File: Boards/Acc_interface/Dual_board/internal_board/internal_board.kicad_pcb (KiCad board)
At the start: 4 copper layers, 85 x 70 mm, 7 parts, among them J2 MM_F_RA_20, J3 MM_F_RA_04, J4 MM_F_RA_14, J5 MM_F_RA_06, J6 MicroFit_RA_10, J7 SS-126-G-2, J8 SS-126-G-2

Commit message: added silkscreen to all acc interface boards
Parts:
- added G***: LOGO, footprints:Olin_O, B.Cu at (134.6, 54.6)
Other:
- board text added: "AIR Control"
- board text added: "Accumulator Interface (Internal) Rev 1 Bryce Mann"
- board text added: "BMS Core"
- board text added: "IMD Latch"
- board text added: "Shutdown"
- board text added: "TSAL"
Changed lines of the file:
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@@
   (general
     (thickness 1.6)
-    (drawings 14)
+    (drawings 20)
     (tracks 149)
     (zones 0)
-    (modules 7)
+    (modules 8)
     (nets 49)
   )
@@
       (net 3 GND))
   )
+  (module footprints:Olin_O (layer B.Cu)
+    (at 134.62 54.61)
+    (fp_text reference G*** (at 10.16 5.08) (layer B.SilkS) hide
+      (effects (font (size 1.524 1.524) (thickness 0.3)) (justify mirror))
+    )
+    (fp_text value LOGO (at 10.16 7.62) (layer B.SilkS) hide
+      (effects (font (size 1.524 1.524) (thickness 0.3)) (justify mirror))
+    )
+    (fp_poly (pts (xy 0.78907 2.933726) (xy 0.297169 2.603291) (xy -0.249654 2.169905) (xy -0.811 1.670573)
+      (xy -1.346471 1.1423) (xy -1.815667 0.622091) (xy -2.036037 0.345931) (xy -2.493304 -0.320664)
+      (xy -2.866143 -0.986545) (xy -3.148527 -1.632052) (xy -3.33443 -2.237523) (xy -3.417825 -2.783297)
+      (xy -3.392687 -3.249711) (xy -3.252989 -3.617104) (xy -3.251451 -3.6195) (xy -3.169272 -3.757194)
+      (xy -3.151881 -3.805837) (xy -3.238357 -3.784085) (xy -3.451232 -3.729169) (xy -3.753084 -3.650766)
+      (xy -3.937 -3.602827) (xy -4.929803 -3.301284) (xy -5.762117 -2.955854) (xy -6.437575 -2.564339)
+      (xy -6.959808 -2.124543) (xy -7.332449 -1.634266) (xy -7.40086 -1.507176) (xy -7.582592 -0.976433)
+      (xy -7.604253 -0.451032) (xy -7.475103 0.063274) (xy -7.204403 0.560731) (xy -6.801416 1.035585)
+      (xy -6.275401 1.482082) (xy -5.63562 1.894469) (xy -4.891334 2.266991) (xy -4.051805 2.593894)
+      (xy -3.126293 2.869426) (xy -2.12406 3.087831) (xy -1.054367 3.243355) (xy 0.073526 3.330246)
+      (xy 0.403482 3.341618) (xy 1.526631 3.369785) (xy 0.78907 2.933726)) (layer B.SilkS) (width 0.01))
+    (fp_poly (pts (xy 3.442983 3.189143) (xy 3.593457 3.149129) (xy 3.859628 3.080824) (xy 4.192829 2.996675)
+      (xy 4.318 2.965353) (xy 4.950523 2.771412) (xy 5.589166 2.511366) (xy 6.187709 2.208074)
+      (xy 6.699928 1.884399) (xy 7.006464 1.635631) (xy 7.427728 1.15255) (xy 7.68721 0.655705)
+      (xy 7.791208 0.151883) (xy 7.746021 -0.352128) (xy 7.557949 -0.849541) (xy 7.23329 -1.333569)
+      (xy 6.778343 -1.797426) (xy 6.199408 -2.234324) (xy 5.502783 -2.637476) (xy 4.694767 -3.000096)
+      (xy 3.78166 -3.315395) (xy 2.769759 -3.576588) (xy 2.037525 -3.718298) (xy 1.579989 -3.791873)
+      (xy 1.263227 -3.832252) (xy 1.062288 -3.841026) (xy 0.952225 -3.819783) (xy 0.916988 -3.789688)
+      (xy 0.858074 -3.735928) (xy 0.847963 -3.779733) (xy 0.766319 -3.839404) (xy 0.537525 -3.878973)
+      (xy 0.3175 -3.891838) (xy -0.049381 -3.903054) (xy -0.420533 -3.915266) (xy -0.613858 -3.922106)
+      (xy -0.848176 -3.919314) (xy -0.993137 -3.895498) (xy -1.016025 -3.876157) (xy -1.081706 -3.846379)
+      (xy -1.164166 -3.861997) (xy -1.171663 -3.848862) (xy -1.054877 -3.771153) (xy -0.838402 -3.644985)
+      (xy -0.801282 -3.624227) (xy -0.008948 -3.11414) (xy 0.773964 -2.467576) (xy 1.356472 -1.894766)
+      (xy 2.033545 -1.129263) (xy 2.578075 -0.383663) (xy 3.016751 0.379744) (xy 3.126149 0.605915)
+      (xy 3.414204 1.311966) (xy 3.572957 1.91735) (xy 3.603305 2.429665) (xy 3.50615 2.856508)
+      (xy 3.413505 3.034819) (xy 3.334494 3.173405) (xy 3.358577 3.208225) (xy 3.442983 3.189143)) (layer B.SilkS) (width 0.01))
+  )
+  (gr_text "Accumulator Interface (Internal)\nRev 1\nBryce Mann" (at 135.89 45.72) (layer B.SilkS)
+    (effects (font (size 1.5 1.5) (thickness 0.3)) (justify mirror))
+  )
+  (gr_text "BMS Core" (at 120.65 64.77) (layer B.SilkS)
+    (effects (font (size 1.5 1.5) (thickness 0.3)) (justify mirror))
+  )
+  (gr_text "IMD Latch" (at 137.16 82.55) (layer B.SilkS)
+    (effects (font (size 1.5 1.5) (thickness 0.3)) (justify mirror))
+  )
+  (gr_text TSAL (at 157.48 45.72) (layer B.SilkS)
+    (effects (font (size 1.5 1.5) (thickness 0.3)) (justify mirror))
+  )
+  (gr_text Shutdown (at 170.18 83.82) (layer B.SilkS)
+    (effects (font (size 1.5 1.5) (thickness 0.3)) (justify mirror))
+  )
+  (gr_text "AIR Control" (at 168.91 72.39) (layer B.SilkS)
+    (effects (font (size 1.5 1.5) (thickness 0.3)) (justify mirror))
+  )
   (gr_arc (start 187.616 103.528) (end 187.616 109.878) (angle -90) (layer Edge.Cuts) (width 0.2))

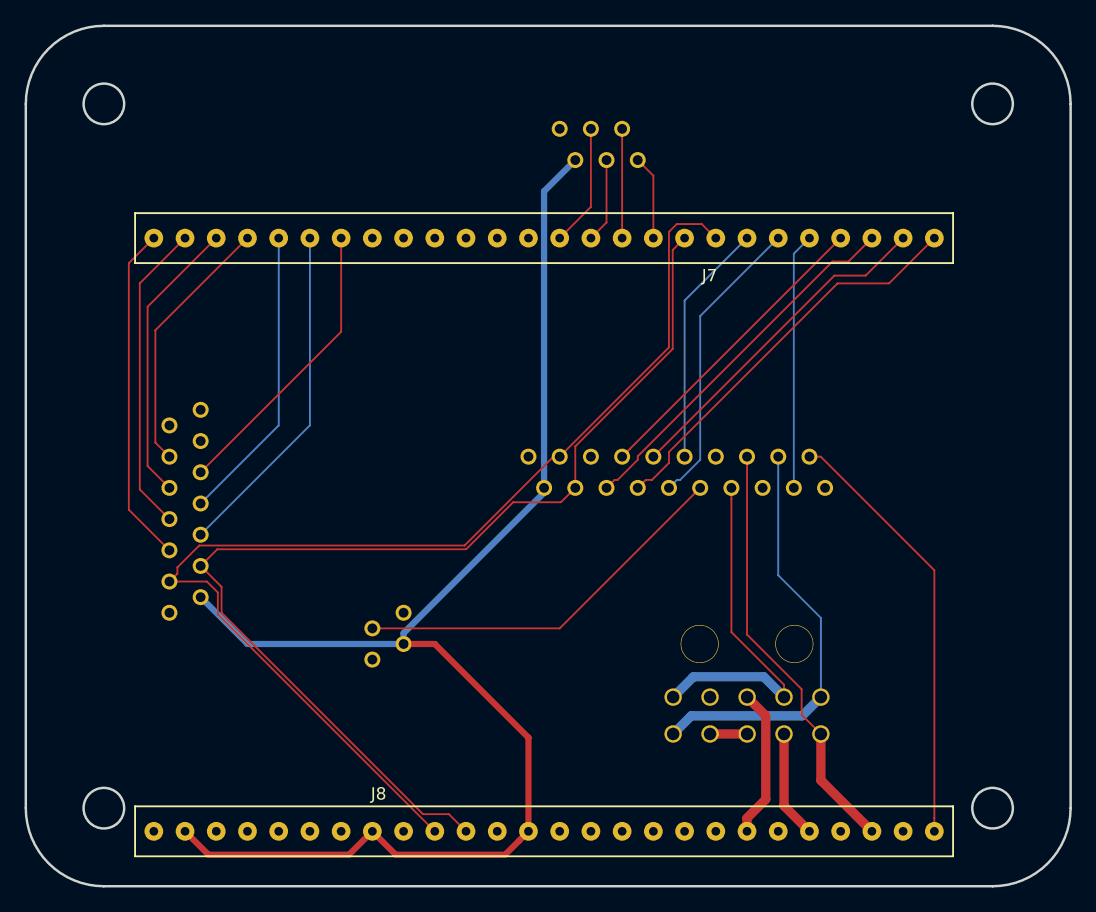
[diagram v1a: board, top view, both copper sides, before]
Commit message: moving connectors for Katya
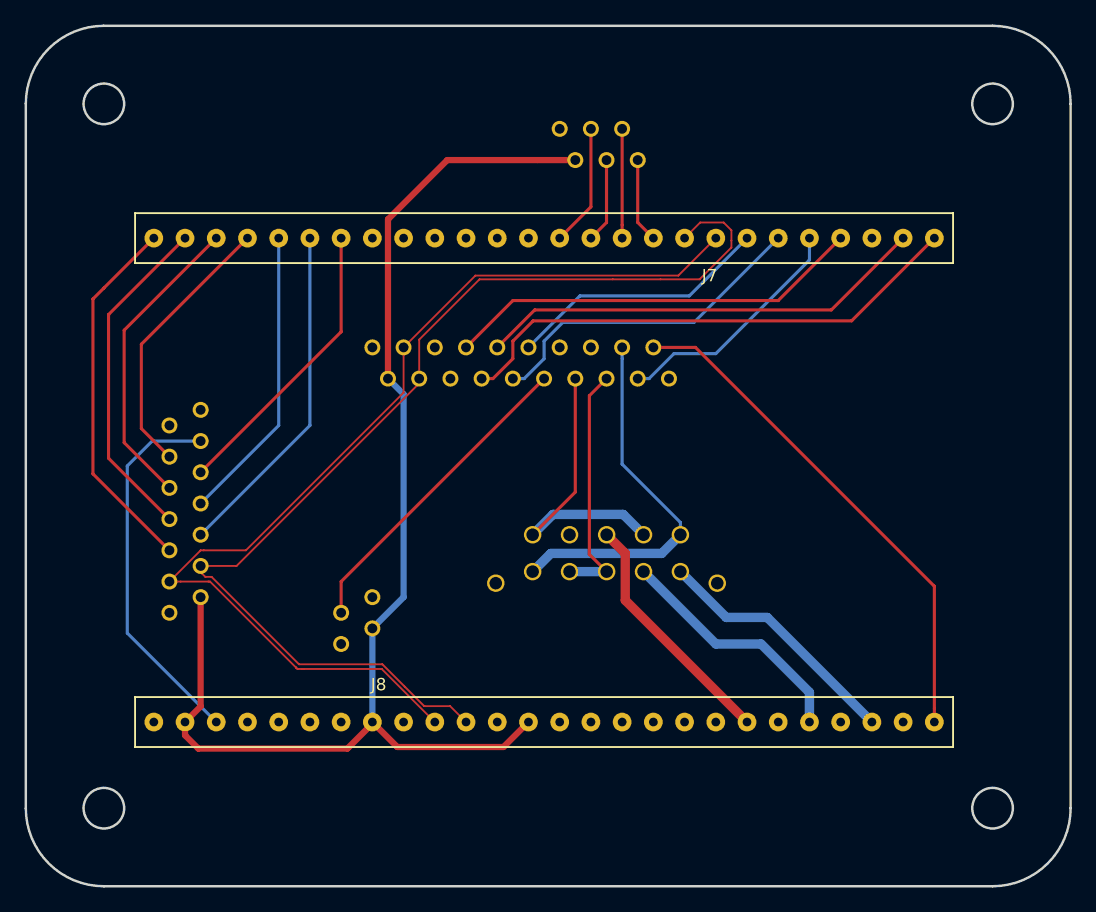
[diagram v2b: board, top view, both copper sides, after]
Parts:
- removed J6: MicroFit_RA_10, footprints:MicroFit_RA_10
- added J1: MicroFit_VT_10, footprints:MicroFit_VT_10, B.Cu at (156.2, 81.3)
- moved J2 15.5 mm to (142.2, 66.0)
- moved J8 8.89 mm to (119.4, 96.5)
- moved J3 2.84 mm to (134.6, 85.1)
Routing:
- net /5V_AIR: track 69.9 -> 86.6 mm
- net /12V: track 115.3 -> 102.4 mm
- net /BMS_SENSE: track 48.1 -> 36.3 mm
- net /Shutdown_E-STOP: track 8.78 -> 20.0 mm
- net /MOSI_AIR: track 30.2 -> 40.8 mm
- net /SCK_AIR: track 33.1 -> 42.4 mm
- net /CAN_HIGH: track 93.8 -> 84.7 mm
- net /RESET_AIR: track 27.7 -> 36.7 mm
- net /MISO_AIR: track 25.1 -> 34.2 mm
- net /Shutdown_Final: track 12.2 -> 20.0 mm
- net /Shutdown_IMD: track 34.7 -> 41.9 mm
- net /Cooling_pressure_sense: track 35.2 -> 42.0 mm
- net /IMD_SENSE: track 31.4 -> 25.9 mm
- net /Shutdown_BMS: track 29.2 -> 24.5 mm
- net /Shutdown_MP: track 34.3 -> 30.5 mm
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
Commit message: Fix ACc interface and add finish AIR mount schematic
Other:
- board text removed: "For Instructional Use Only."
- board text removed: "SOLIDWORKS Educational Product."
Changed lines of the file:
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@@
-(kicad_pcb (version 20171130) (host pcbnew 5.0.2-bee76a0~70~ubuntu16.04.1)
+(kicad_pcb (version 20171130) (host pcbnew 5.0.2-bee76a0~70~ubuntu18.04.1)
   (general
     (thickness 1.6)
-    (drawings 20)
+    (drawings 18)
     (tracks 173)
     (zones 0)
@@
   )
   (setup
-    (last_trace_width 0.254)
+    (last_trace_width 0.1524)
     (user_trace_width 0.1524)
     (user_trace_width 0.254)
@@
     (pcbplotparams
       (layerselection 0x010fc_ffffffff)
-      (usegerberextensions false)
+      (usegerberextensions true)
       (usegerberattributes false)
       (usegerberadvancedattributes false)
@@
       (outputformat 1)
       (mirror false)
-      (drillshape 1)
+      (drillshape 0)
       (scaleselection 1)
-      (outputdirectory ""))
+      (outputdirectory "gerb/"))
   )
   (net 0 "")
@@
   (gr_arc (start 115.316 103.528) (end 108.966 103.528) (angle -90) (layer Edge.Cuts) (width 0.2))
   (gr_line (start 108.966 103.528) (end 108.966 46.228) (layer Edge.Cuts) (width 0.2))
-  (gr_text "SOLIDWORKS Educational Product." (at 108.966 110.897566) (layer Edge.Cuts)
-    (effects (font (size 4.83362 3.866896) (thickness 0.2)) (justify left top))
-  )
   (gr_circle (center 187.616 103.528) (end 189.267 103.528) (layer Edge.Cuts) (width 0.2))
   (gr_circle (center 115.316 103.528) (end 116.967 103.528) (layer Edge.Cuts) (width 0.2))
   (gr_line (start 187.616 109.878) (end 115.316 109.878) (layer Edge.Cuts) (width 0.2))
-  (gr_text "For Instructional Use Only." (at 108.966 118.147996) (layer Edge.Cuts)
-    (effects (font (size 4.83362 3.866896) (thickness 0.2)) (justify left top))
-  )
   (gr_arc (start 187.616 46.228) (end 193.966 46.228) (angle -90) (layer Edge.Cuts) (width 0.2))
   (gr_line (start 193.966 46.228) (end 193.966 103.528) (layer Edge.Cuts) (width 0.2))
@@
     (polygon
       (pts
-        (xy 118.11 41.91) (xy 118.11 107.95) (xy 184.15 107.95) (xy 184.15 41.91)
+        (xy 100.1014 34.544) (xy 106.0196 112.7506) (xy 199.1614 113.2586) (xy 199.7456 37.7698)
       )
     )

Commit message: Modify Acc interface and AIR Mount
Add emeter lines to the dual mounting Accumulator interface boards
fix resistor on AIR mount board for new 500V rates TSMP resistor
Exported and shipped both
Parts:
- added J6: MicroFit_V_2, footprints:MicroFit_V_2, B.Cu at (188.7, 73.2)
- added J9: MicroFit_V_2, footprints:MicroFit_V_2, B.Cu at (178.4, 73.2)
- moved G*** 38.8 mm to (173.0, 48.8)
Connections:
- J8 pad 17: Net-(J8-Pad17) -> /emeter_CAN_HIGH
- J8 pad 19: Net-(J8-Pad19) -> /emeter_CAN_LOW
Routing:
- net /12V: track 102.4 -> 162.0 mm
- net /emeter_CAN_LOW: track 0.00 -> 56.1 mm
- net /emeter_CAN_HIGH: track 0.00 -> 53.1 mm
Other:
- outline, holes or cut-outs redrawn
- board text added: "12V"
- board text added: "Accumulator Interface (Internal) Rev 2 Bryce Mann Corey Cochran-Lepiz"
- board text added: "CAN High"
- board text added: "CAN Low"
- board text added: "Energy-Meter"
- board text added: "GND"
- board text removed: "Accumulator Interface (Internal) Rev 1 Bryce Mann"
